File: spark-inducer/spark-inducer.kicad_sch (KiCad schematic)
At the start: 72 parts, among them J1 POWER IN, J10 IO_A_1, J11 IO_A_3, J12 IO_A_2, J13 IO_A_4, J14 IO_B_1, J15 IO_B_3, J16 IO_B_2, J17 IO_B_4, J18 REF_SELECT, J19 POWER_A_1, J2 IO1, J20 POWER_A_2, J21 POWER_A_3, J22 POWER_A_4, J23 POWER_B_1, J24 POWER_B_2, J25 POWER_B_3, J26 POWER_B_4, J3 IO2, J4 IO3, J5 IO4, J6 IO5, J7 IO6, J8 OUT1, J9 OUT2, SW1 SWITCH, U1 TL072B, U2 TL072B, U3 TL431B, U4 L78LXX, U5 LM4040, U6 REF50XX

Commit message: Update all footprints, use new custom footprints
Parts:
- removed J1: POWER IN, Protorack:Samtec_HTST-108-01-T-DV, symbol Connector_Generic:Conn_02x08_Odd_Even
- added H1: SCREW_SW_TOP, Protorack:Screw_ISO4762_M2x6, symbol Protorack:Screw
- added H10: NUT_OUT1, Protorack:Nut_M6x2mm_Knurled, symbol Protorack:Nut
- added H11: NUT_IO2, Protorack:Nut_M6x2mm_Knurled, symbol Protorack:Nut
- added H12: NUT_IO4, Protorack:Nut_M6x2mm_Knurled, symbol Protorack:Nut
- added H13: NUT_IO6, Protorack:Nut_M6x2mm_Knurled, symbol Protorack:Nut
- added H14: NUT_OUT2, Protorack:Nut_M6x2mm_Knurled, symbol Protorack:Nut
- added H15: NUT_POT_A, Protorack:Nut_M7x2mm_Black, symbol Protorack:Nut
- added H16: NUT_POT_B, Protorack:Nut_M7x2mm_Black, symbol Protorack:Nut
- added H17: NUT_POT_C, Protorack:Nut_M7x2mm_Black, symbol Protorack:Nut
- added H18: NUT_POT_D, Protorack:Nut_M7x2mm_Black, symbol Protorack:Nut
- added H19: WASHER_POT_A, Protorack:Washer_RV16AF_2mm_Tab, symbol Protorack:Washer
- added H2: SCREW_SW_BOT, Protorack:Screw_ISO4762_M2x6, symbol Protorack:Screw
- added H20: WASHER_POT_B, Protorack:Washer_RV16AF_2mm_Tab, symbol Protorack:Washer
- added H21: WASHER_POT_C, Protorack:Washer_RV16AF_2mm_Tab, symbol Protorack:Washer
- added H22: WASHER_POT_D, Protorack:Washer_RV16AF_2mm_Tab, symbol Protorack:Washer
- added H3: SCREW_PANEL_TL, Protorack:Screw_ISO7380_M3x6, symbol Protorack:Screw
- added H4: SCREW_PANEL_TR, Protorack:Screw_ISO7380_M3x6, symbol Protorack:Screw
- added H5: SCREW_PANEL_BL, Protorack:Screw_ISO7380_M3x6, symbol Protorack:Screw
- added H6: SCREW_PANEL_BR, Protorack:Screw_ISO7380_M3x6, symbol Protorack:Screw
- added H7: NUT_IO1, Protorack:Nut_M6x2mm_Knurled, symbol Protorack:Nut
- added H8: NUT_IO3, Protorack:Nut_M6x2mm_Knurled, symbol Protorack:Nut
- added H9: NUT_IO5, Protorack:Nut_M6x2mm_Knurled, symbol Protorack:Nut
- added J1: Eurorack_Power_Header, Protorack:Eurorack_Power_Header_2x08_SMD_HandSolder, symbol Protorack:Eurorack_Power_Header
- J10, J11, J12, J13, J14, J15, J16, J17: footprint Protorack:Samtec_TSW-106-09-T-S-RA_Shortened_SurfaceMount -> Protorack:Samtec_TSW-106-09-T-S-RA_Shortened_SMD
- J2, J3, J4, J5, J6, J7, J8, J9: footprint Protorack:QingPu_WQP-PJ376M_SurfaceMount -> Protorack:QingPu_WQP-WQP518MA-BM_SMD
- R10, R11: value 18k -> 33k 0.1%
- RV1, RV2, RV3, RV4: footprint Protorack:Alpha_RV16AF-20-15F_SurfaceMount_Nut_Knob -> Protorack:Alpha_RV16AF-10-17K_SMD_Slot; symbol Device:R_POT -> Device:R_Potentiometer
- SW1: value SWITCH -> (none); footprint Protorack:CW_GF-161-3011_SurfaceMount -> (none); symbol Protorack:SW_3PST_x3 -> Protorack:SW_3PST
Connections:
- net +12V_IN: now also J1.+12V
- net +5V_IN: now also J1.+5VD
- net -12V_IN: now also J1.-12V
- net GND: now also J1.GND
- no-connect marks 2 -> 4
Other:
- moved on the sheet: TP1, TP2

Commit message: Fix breadboard spacings, Add glue marks
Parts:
- added H23: (no value), symbol Protorack:Breadboard_MB-102
- added H24: (no value), Protorack:Breadboard_MB-102, symbol Protorack:Breadboard_MB-102
- C5, C6, C7, C8: footprint Capacitor_SMD:C_1206_3216Metric_Pad1.42x1.75mm_HandSolder -> (none)
- SW1: value (none) -> SWITCH; footprint (none) -> Protorack:CW_GF-161-3011_SMD
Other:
- moved on the sheet: H1, H2
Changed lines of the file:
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@@
       (effects (font (size 1.27 1.27)) (justify left))
     )
-    (property "Footprint" "Capacitor_SMD:C_1206_3216Metric_Pad1.42x1.75mm_HandSolder" (id 2) (at 61.9252 35.56 0)
+    (property "Footprint" "" (id 2) (at 61.9252 35.56 0)
       (effects (font (size 1.27 1.27)) hide)
     )
@@
       (effects (font (size 1.27 1.27)) (justify left))
     )
-    (property "Footprint" "Capacitor_SMD:C_1206_3216Metric_Pad1.42x1.75mm_HandSolder" (id 2) (at 61.9252 66.04 0)
+    (property "Footprint" "" (id 2) (at 61.9252 66.04 0)
       (effects (font (size 1.27 1.27)) hide)
     )
@@
       (effects (font (size 1.27 1.27)) (justify left))
     )
-    (property "Footprint" "Capacitor_SMD:C_1206_3216Metric_Pad1.42x1.75mm_HandSolder" (id 2) (at 61.9252 96.52 0)
+    (property "Footprint" "" (id 2) (at 61.9252 96.52 0)
       (effects (font (size 1.27 1.27)) hide)
     )
@@
       (effects (font (size 1.27 1.27)) (justify right))
     )
-    (property "Footprint" "Capacitor_SMD:C_1206_3216Metric_Pad1.42x1.75mm_HandSolder" (id 2) (at 142.5448 144.78 0)
+    (property "Footprint" "" (id 2) (at 142.5448 144.78 0)
       (effects (font (size 1.27 1.27)) hide)
     )
@@
     (in_bom yes) (on_board yes)
     (property "Reference" "SW1" (id 0) (at 33.02 19.05 0))
-    (property "Value" "" (id 1) (at 33.02 21.59 0))
-    (property "Footprint" "" (id 2) (at 33.02 25.4 0)
+    (property "Value" "SWITCH" (id 1) (at 33.02 21.59 0))
+    (property "Footprint" "Protorack:CW_GF-161-3011_SMD" (id 2) (at 33.02 25.4 0)
       (effects (font (size 1.27 1.27)) hide)
     )
@@
     (in_bom yes) (on_board yes)
     (property "Reference" "SW1" (id 0) (at 33.02 49.53 0))
-    (property "Value" "" (id 1) (at 33.02 52.07 0))
-    (property "Footprint" "" (id 2) (at 33.02 55.88 0)
+    (property "Value" "SWITCH" (id 1) (at 33.02 52.07 0))
+    (property "Footprint" "Protorack:CW_GF-161-3011_SMD" (id 2) (at 33.02 55.88 0)
       (effects (font (size 1.27 1.27)) hide)
     )
@@
     (in_bom yes) (on_board yes)
     (property "Reference" "SW1" (id 0) (at 33.02 80.01 0))
-    (property "Value" "" (id 1) (at 33.02 82.55 0))
-    (property "Footprint" "" (id 2) (at 33.02 86.36 0)
+    (property "Value" "SWITCH" (id 1) (at 33.02 82.55 0))
+    (property "Footprint" "Protorack:CW_GF-161-3011_SMD" (id 2) (at 33.02 86.36 0)
       (effects (font (size 1.27 1.27)) hide)
     )
@@
     )
   )
-  (symbol (lib_id "Protorack:Screw") (at 85.09 170.18 180) (unit 1)
-    (in_bom yes) (on_board yes)
-    (property "Reference" "H2" (id 0) (at 87.63 168.91 0)
-      (effects (font (size 1.27 1.27)) (justify right))
-    )
-    (property "Value" "SCREW_SW_BOT" (id 1) (at 87.63 171.45 0)
-      (effects (font (size 1.27 1.27)) (justify right))
-    )
-    (property "Footprint" "Protorack:Screw_ISO4762_M2x6" (id 2) (at 85.09 170.18 0)
-      (effects (font (size 1.27 1.27)) hide)
-    )
-    (property "Datasheet" "" (id 3) (at 85.09 170.18 0)
+  (symbol (lib_id "Protorack:Screw") (at 107.95 170.18 180) (unit 1)
+    (in_bom yes) (on_board yes)
+    (property "Reference" "H2" (id 0) (at 110.49 168.91 0)
+      (effects (font (size 1.27 1.27)) (justify right))
+    )
+    (property "Value" "SCREW_SW_BOT" (id 1) (at 110.49 171.45 0)
+      (effects (font (size 1.27 1.27)) (justify right))
+    )
+    (property "Footprint" "Protorack:Screw_ISO4762_M2x6" (id 2) (at 107.95 170.18 0)
+      (effects (font (size 1.27 1.27)) hide)
+    )
+    (property "Datasheet" "" (id 3) (at 107.95 170.18 0)
       (effects (font (size 1.27 1.27)) hide)
     )
@@
     )
   )
+  (symbol (lib_id "Protorack:Breadboard_MB-102") (at 83.82 165.1 0) (unit 1)
+    (in_bom yes) (on_board yes) (fields_autoplaced)
+    (property "Reference" "H23" (id 0) (at 87.63 163.8299 0)
+      (effects (font (size 1.27 1.27)) (justify left))
+    )
+    (property "Value" "" (id 1) (at 87.63 166.3699 0)
+      (effects (font (size 1.27 1.27)) (justify left))
+    )
+    (property "Footprint" "" (id 2) (at 83.82 165.1 0)
+      (effects (font (size 1.27 1.27)) hide)
+    )
+    (property "Datasheet" "" (id 3) (at 83.82 165.1 0)
+      (effects (font (size 1.27 1.27)) hide)
+    )
+  )
   (symbol (lib_id "Protorack:Screw") (at 85.09 182.88 180) (unit 1)
     (in_bom yes) (on_board yes)
@@
     )
   )
-  (symbol (lib_id "Protorack:Screw") (at 85.09 165.1 180) (unit 1)
-    (in_bom yes) (on_board yes)
-    (property "Reference" "H1" (id 0) (at 87.63 163.83 0)
-      (effects (font (size 1.27 1.27)) (justify right))
-    )
-    (property "Value" "SCREW_SW_TOP" (id 1) (at 87.63 166.37 0)
-      (effects (font (size 1.27 1.27)) (justify right))
-    )
-    (property "Footprint" "Protorack:Screw_ISO4762_M2x6" (id 2) (at 85.09 165.1 0)
-      (effects (font (size 1.27 1.27)) hide)
-    )
-    (property "Datasheet" "" (id 3) (at 85.09 165.1 0)
+  (symbol (lib_id "Protorack:Screw") (at 107.95 165.1 180) (unit 1)
+    (in_bom yes) (on_board yes)
+    (property "Reference" "H1" (id 0) (at 110.49 163.83 0)
+      (effects (font (size 1.27 1.27)) (justify right))
+    )
+    (property "Value" "SCREW_SW_TOP" (id 1) (at 110.49 166.37 0)
+      (effects (font (size 1.27 1.27)) (justify right))
+    )
+    (property "Footprint" "Protorack:Screw_ISO4762_M2x6" (id 2) (at 107.95 165.1 0)
+      (effects (font (size 1.27 1.27)) hide)
+    )
+    (property "Datasheet" "" (id 3) (at 107.95 165.1 0)
       (effects (font (size 1.27 1.27)) hide)
     )
@@
     )
     (property "Datasheet" "" (id 3) (at 139.7 182.88 0)
+      (effects (font (size 1.27 1.27)) hide)
+    )
+  )
+  (symbol (lib_id "Protorack:Breadboard_MB-102") (at 83.82 170.18 0) (unit 1)
+    (in_bom yes) (on_board yes) (fields_autoplaced)
+    (property "Reference" "H24" (id 0) (at 87.63 168.9099 0)
+      (effects (font (size 1.27 1.27)) (justify left))
+    )
+    (property "Value" "" (id 1) (at 87.63 171.4499 0)
+      (effects (font (size 1.27 1.27)) (justify left))
+    )
+    (property "Footprint" "Protorack:Breadboard_MB-102" (id 2) (at 83.82 170.18 0)
+      (effects (font (size 1.27 1.27)) hide)
+    )
+    (property "Datasheet" "" (id 3) (at 83.82 170.18 0)
       (effects (font (size 1.27 1.27)) hide)
     )
@@
     )
     (path "/00000000-0000-0000-0000-00006187b993"
-      (reference "C5") (unit 1) (value "10uF") (footprint "Capacitor_SMD:C_1206_3216Metric_Pad1.42x1.75mm_HandSolder")
+      (reference "C5") (unit 1) (value "10uF") (footprint "Capacitor_SMD:C_1206_3216Metric_Pad1.33x1.80mm_HandSolder")
     )
     (path "/00000000-0000-0000-0000-00006188e101"
-      (reference "C6") (unit 1) (value "10uF") (footprint "Capacitor_SMD:C_1206_3216Metric_Pad1.42x1.75mm_HandSolder")
+      (reference "C6") (unit 1) (value "10uF") (footprint "Capacitor_SMD:C_1206_3216Metric_Pad1.33x1.80mm_HandSolder")
     )
     (path "/00000000-0000-0000-0000-00006188fca9"
-      (reference "C7") (unit 1) (value "10uF") (footprint "Capacitor_SMD:C_1206_3216Metric_Pad1.42x1.75mm_HandSolder")
+      (reference "C7") (unit 1) (value "10uF") (footprint "Capacitor_SMD:C_1206_3216Metric_Pad1.33x1.80mm_HandSolder")
     )
     (path "/00000000-0000-0000-0000-000061d43a49"
-      (reference "C8") (unit 1) (value "10uF") (footprint "Capacitor_SMD:C_1206_3216Metric_Pad1.42x1.75mm_HandSolder")
+      (reference "C8") (unit 1) (value "10uF") (footprint "Capacitor_SMD:C_1206_3216Metric_Pad1.33x1.80mm_HandSolder")
     )
     (path "/00000000-0000-0000-0000-000061930fce"
@@
       (reference "H22") (unit 1) (value "WASHER_POT_D") (footprint "Protorack:Washer_RV16AF_2mm_Tab")
     )
+    (path "/360833b2-d937-485f-8f4a-6c8513d07533"
+      (reference "H23") (unit 1) (value "BREADBOARD_TOP") (footprint "Protorack:Breadboard_MB-102")
+    )
+    (path "/7d596273-21ce-44a5-b713-91e59863afb2"
+      (reference "H24") (unit 1) (value "BREADBOARD_BOT") (footprint "Protorack:Breadboard_MB-102")
+    )
     (path "/11a1f7b5-66db-4e36-8977-92743aadb517"

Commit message: Add knobs
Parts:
- added H25, H26, H27, H28: (no value), symbol Protorack:Knob
- C5, C6, C7, C8: footprint (none) -> Capacitor_SMD:C_1206_3216Metric_Pad1.33x1.80mm_HandSolder
- H23: value (none) -> BREADBOARD_TOP; footprint (none) -> Protorack:Breadboard_MB-102
- H24: value (none) -> BREADBOARD_BOT
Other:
- moved on the sheet: C8, R4, R5, R6, R7, R8, U1A, U1B, U3

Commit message: Add ground clip attachment point, test points, rubber feet
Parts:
- added H29: FOOT_TL, Protorack:3M_SJ-5023, symbol Protorack:Rubber_Foot
- added H30: FOOT_BL, Protorack:3M_SJ-5023, symbol Protorack:Rubber_Foot
- added H31: FOOT_TR, Protorack:3M_SJ-5023, symbol Protorack:Rubber_Foot
- added H32: FOOT_BR, Protorack:3M_SJ-5023, symbol Protorack:Rubber_Foot
- added TP3: +5V, TestPoint:TestPoint_Pad_D1.5mm, symbol Connector:TestPoint
- added TP4: +12V, TestPoint:TestPoint_Pad_D1.5mm, symbol Connector:TestPoint
- added TP5, TP8: GND, TestPoint:TestPoint_Pad_D1.5mm, symbol Connector:TestPoint
- added TP6: -12V, TestPoint:TestPoint_Pad_D1.5mm, symbol Connector:TestPoint
- added TP7: +REF, TestPoint:TestPoint_Pad_D1.5mm, symbol Connector:TestPoint
- added TP9: -REF, TestPoint:TestPoint_Pad_D1.5mm, symbol Connector:TestPoint
- D1, D2, D3: footprint LED_SMD:LED_1206_3216Metric_Pad1.42x1.75mm_HandSolder -> Protorack:LED_1206_3216Metric_ReverseMount_HandSolder
- D4, D5, D6: footprint Diode_SMD:D_SOD-123 -> Protorack:D_SOD-123
- F1: value 1206L020 -> 200mA
- F2, F3: value 1206L020 -> 100mA
- H1, H2: footprint Protorack:Screw_ISO4762_M2x6 -> Protorack:Screw_ISO7380_M2-5x6
- H25: value (none) -> KNOB_POT_A; footprint (none) -> Protorack:Sifam_3-03-TPN130-006
- H26: value (none) -> KNOB_POT_B; footprint (none) -> Protorack:Sifam_3-03-TPN130-006
- H27: value (none) -> KNOB_POT_C; footprint (none) -> Protorack:Sifam_3-03-TPN130-006
- H28: value (none) -> KNOB_POT_D; footprint (none) -> Protorack:Sifam_3-03-TPN130-006
- U1, U2: value TL072B -> TL072H
- U4: value L78LXX -> L78Lxx; footprint Package_TO_SOT_SMD:SOT-89-3 -> Protorack:SOT-89-3_ThermalReliefs
- U6: value REF50XX -> REF50xx
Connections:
- net +12V: now also TP4.1
- net +5V: now also TP3.1
- net +REF: now also TP7.1
- net -12V: now also TP6.1
- net -REF: now also TP9.1
- net GND: now also TP5.1, TP8.1
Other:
- note added: "10k for 2.5V => IL + IZ = ~1mA 2.2k for 5V => IL + IZ = ~1.5mA 1k for 10V => IL + IZ = ~2mA"
- note removed: "2.2k for 5V 1k for 10V"
- moved on the sheet: C1, C2, C3, C4, D1, D2, D3, H1, H2, H23, H24, J1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

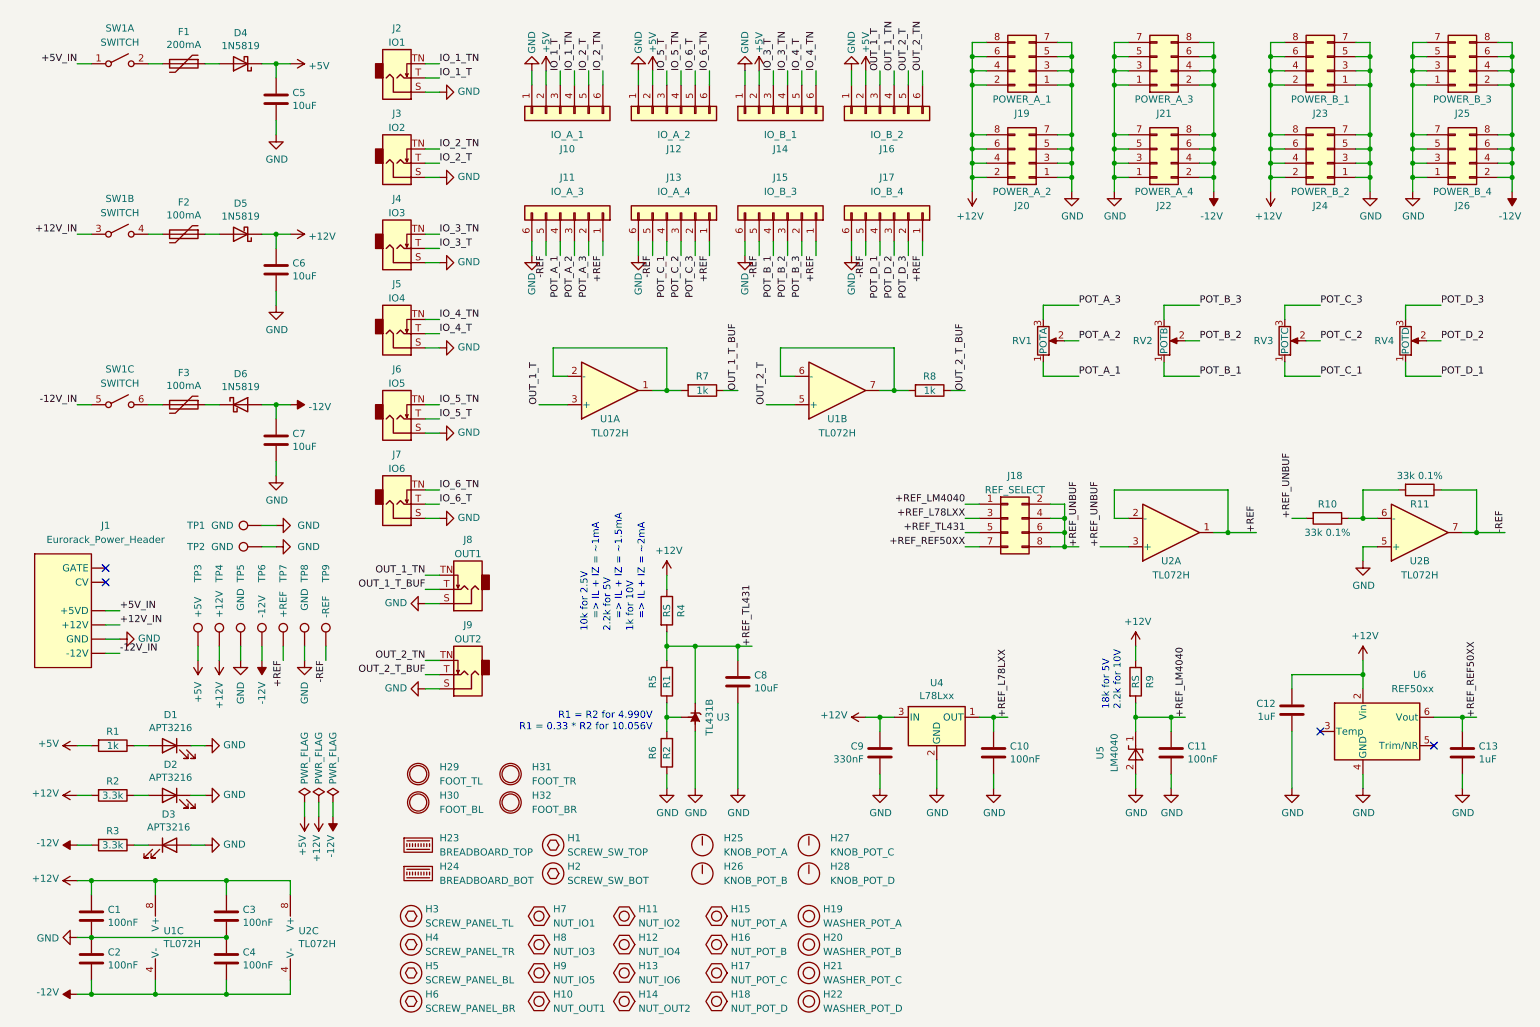
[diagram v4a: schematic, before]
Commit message: Update files to KiCad 7, Fix edge clearance, Add more spokes to washers
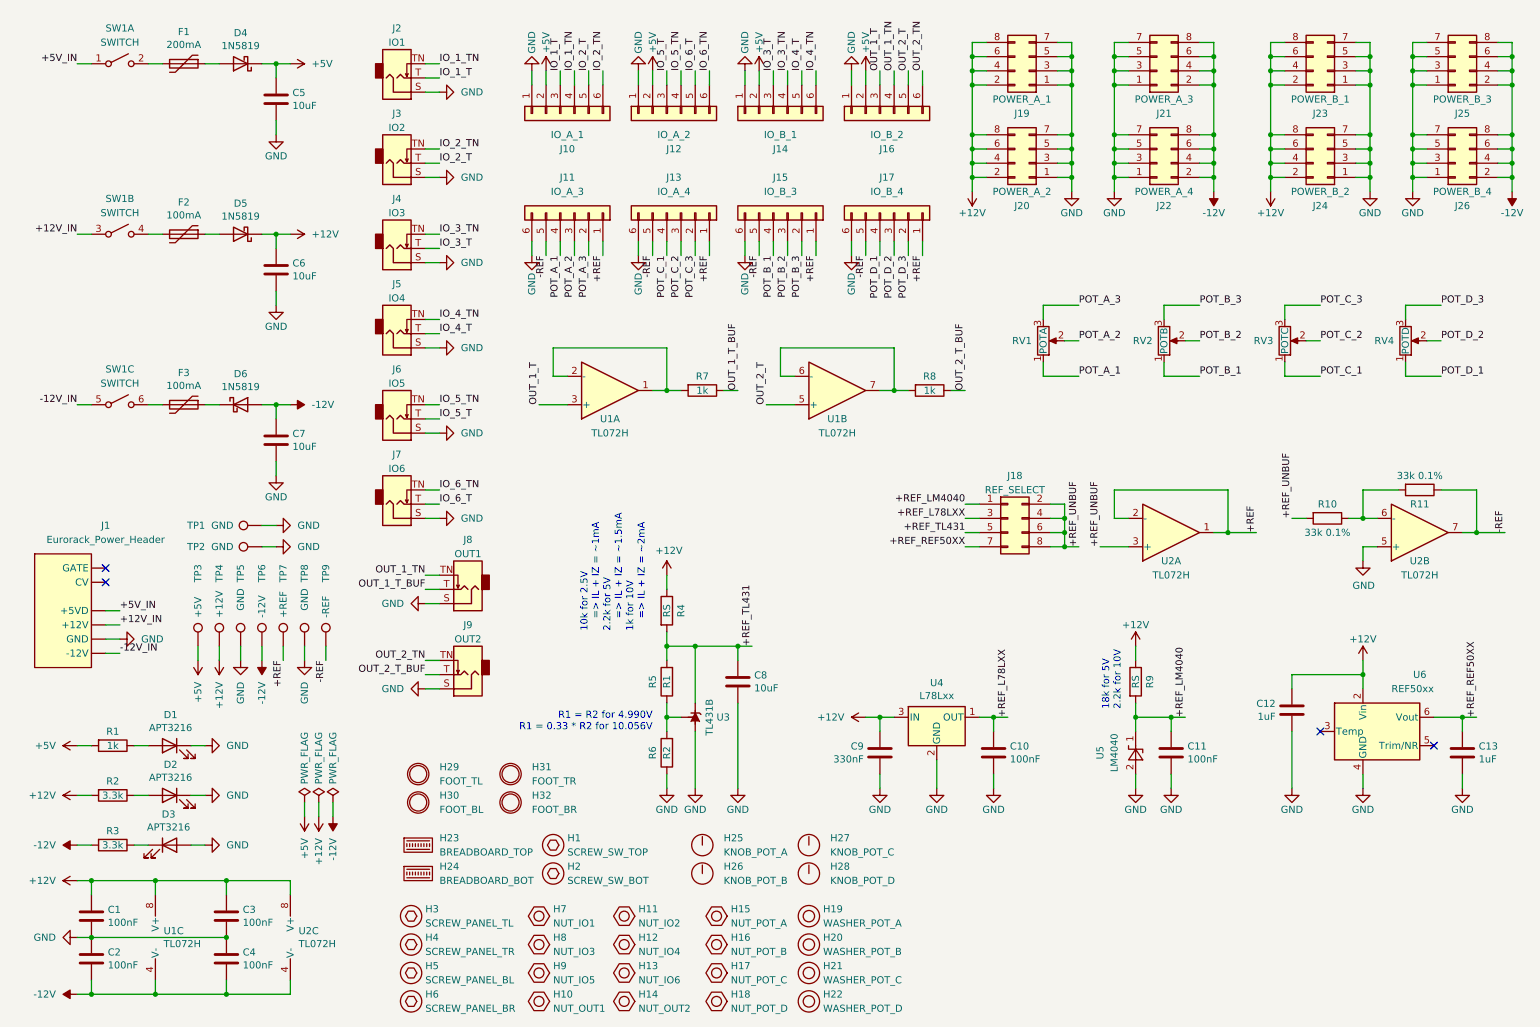
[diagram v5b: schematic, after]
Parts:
- J2, J3, J4, J5, J6, J7, J8, J9: symbol Connector:AudioJack2_SwitchT -> Connector_Audio:AudioJack2_SwitchT
